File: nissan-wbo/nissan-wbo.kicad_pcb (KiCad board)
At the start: 2 copper layers, 21.9 x 15.8 mm, 26 parts, among them J1 Conn_01x02, J2 Conn_01x03, U1 MCP6004

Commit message: LCSC
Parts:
- added C4: 100n, Capacitor_SMD:C_0603_1608Metric, F.Cu at (58.1, 99.4)
- C1, C8: footprint Capacitor_SMD:C_0402_1005Metric -> Capacitor_SMD:C_0603_1608Metric
- R8: footprint Resistor_SMD:R_0402_1005Metric -> Resistor_SMD:R_0603_1608Metric
- moved C8 1.42 mm to (58.5, 97.7)
- moved R8 0.86 mm to (61.1, 87.8)
- moved C1 0.20 mm to (57.7, 90.8), turned to 90 degrees
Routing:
- net Net-(J2-Pad2): track 2.74 -> 9.61 mm
- net +5V: track 17.2 -> 18.7 mm
- net Net-(C8-Pad1): track 20.1 -> 21.5 mm
- net Net-(C8-Pad2): track 7.39 -> 8.42 mm
- net Net-(C6-Pad1): track 3.75 -> 4.50 mm

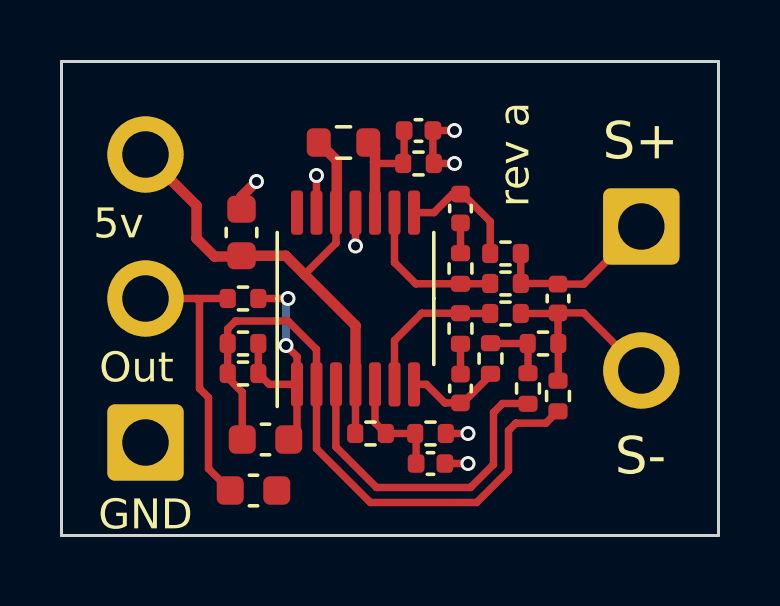
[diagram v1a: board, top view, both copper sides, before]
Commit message: add via (C4, GND) and export gerbers
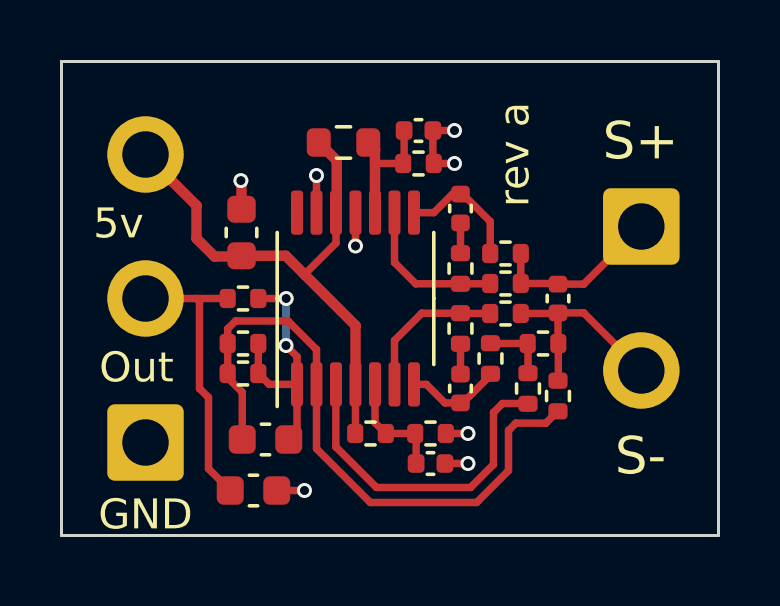
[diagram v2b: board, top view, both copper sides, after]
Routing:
- net GND: track 7.51 -> 8.27 mm, vias 7 -> 8

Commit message: fix silk
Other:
- board text added: "rev b"
- board text removed: "rev a"
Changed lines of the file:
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@@
     (effects (font (size 1 1) (thickness 0.15)) (justify mirror))
   )
-  (gr_text "rev a" (at 66.8 88.2 90) (layer "F.SilkS")
+  (gr_text "rev b" (at 66.8 88.2 90) (layer "F.SilkS")
     (effects (font (size 1 1) (thickness 0.15)))
   )
@@
     (effects (font (size 1 1) (thickness 0.15)))
   )
-  (gr_text "S-" (at 71 98.25) (layer "F.SilkS")
+  (gr_text "S+" (at 71 98.25) (layer "F.SilkS")
     (effects (font (size 1.25 1.25) (thickness 0.2)))
   )
@@
     (effects (font (size 1 1) (thickness 0.15)))
   )
-  (gr_text "S+" (at 71 87.75) (layer "F.SilkS")
+  (gr_text "S-" (at 71 87.75) (layer "F.SilkS")
     (effects (font (size 1.25 1.25) (thickness 0.2)))
   )
